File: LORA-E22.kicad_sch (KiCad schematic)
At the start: 22 parts, among them J5 Conn_Coaxial, U3 E22P-915M30S

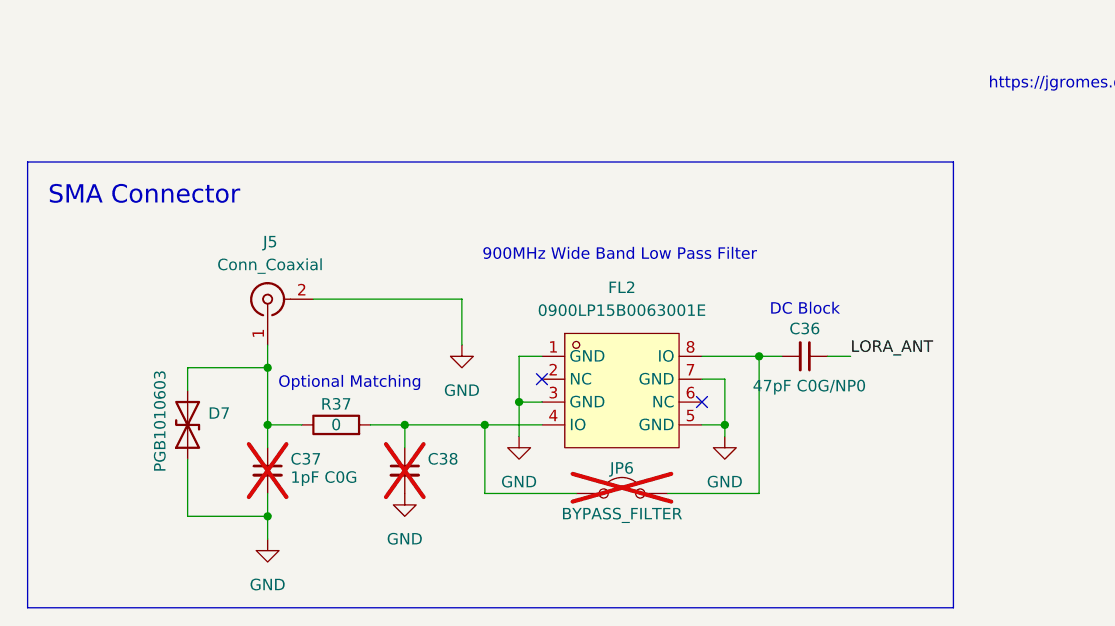
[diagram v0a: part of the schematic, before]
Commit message: wired BQ25798 schematic
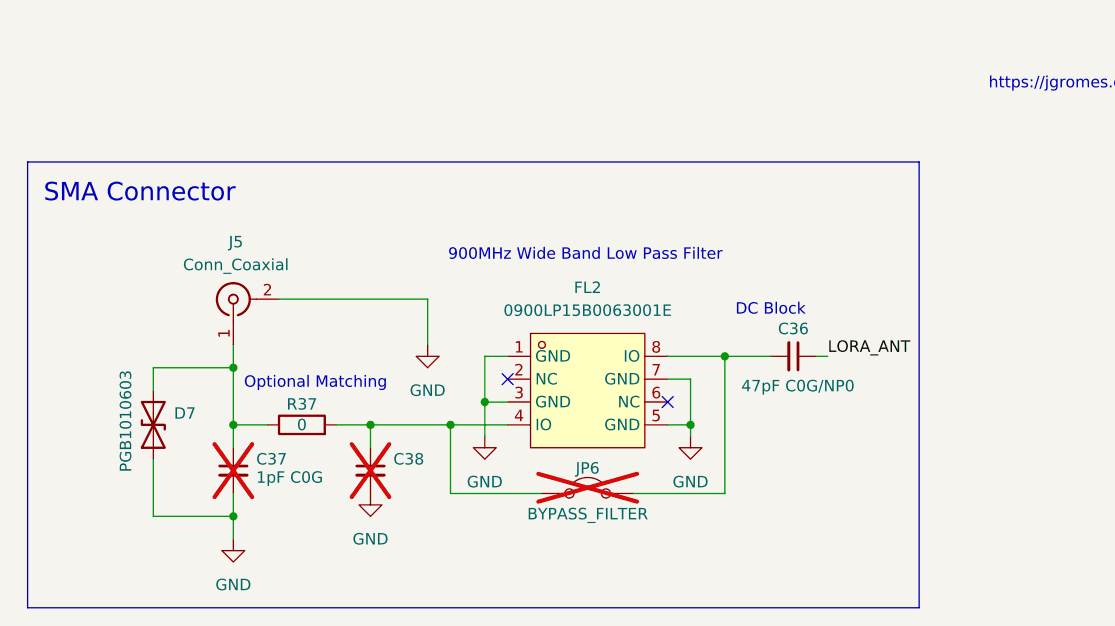
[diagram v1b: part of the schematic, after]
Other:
- moved on the sheet: C36, C37, C38, D7, FL2, J5, JP6, R37

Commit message: changes
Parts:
- added FB1: 1A, symbol Device:FerriteBead
- added JP8: FB_JUMP, Jumper:SolderJumper-2_P1.3mm_Open_RoundedPad1.0x1.5mm, symbol Jumper:SolderJumper_2_Open
- added R73: 5, Capacitor_SMD:C_0603_1608Metric_Pad1.08x0.95mm_HandSolder, symbol Device:R_Small
- added TP7: 5V_LORA, TestPoint:TestPoint_2Pads_Pitch2.54mm_Drill0.8mm, symbol Connector:TestPoint_2Pole
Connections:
- net +5V: now also FB1.1, JP8.2 (B), R73.1; no longer C12.1, C13.1, C14.1, C15.1, C18.1, C26.1, C29.1, D9.2 (A2), U3.10 (VCC), U3.9 (VCC)
- net GND: now also TP7.2
- new net: C12.1, C13.1, C14.1, C15.1, C18.1, C26.1, C29.1, D9.2 (A2), FB1.2, JP8.1 (A), R73.2, TP7.1, U3.10 (VCC), U3.9 (VCC)
